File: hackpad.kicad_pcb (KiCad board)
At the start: 2 copper layers, 79 x 101 mm, 50 parts, among them J1 Conn_01x04, SW1 SW_Push, SW10 SW_Push, SW11 SW_Push, SW12 SW_Push, SW13 SW_Push, SW14 SW_Push, SW15 SW_Push, SW16 SW_Push, SW2 SW_Push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

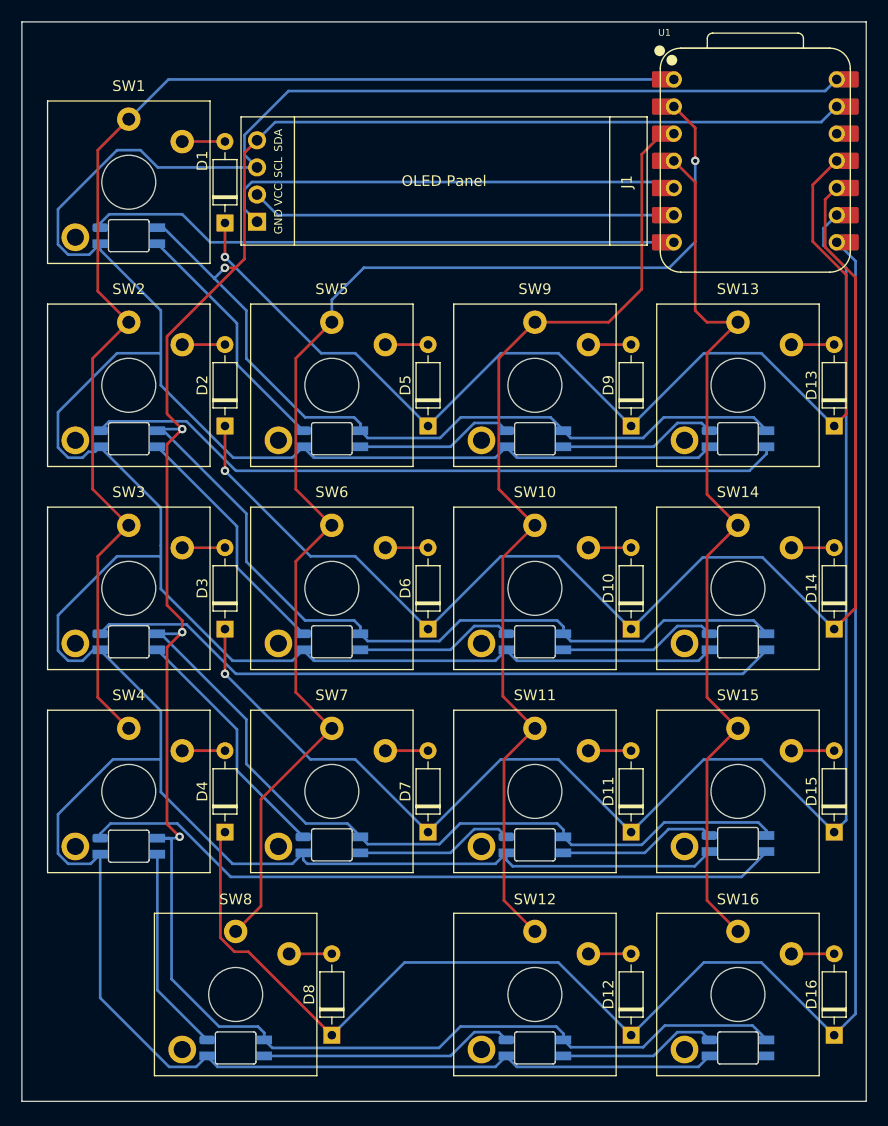
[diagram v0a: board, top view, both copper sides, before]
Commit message: add branding to pcb
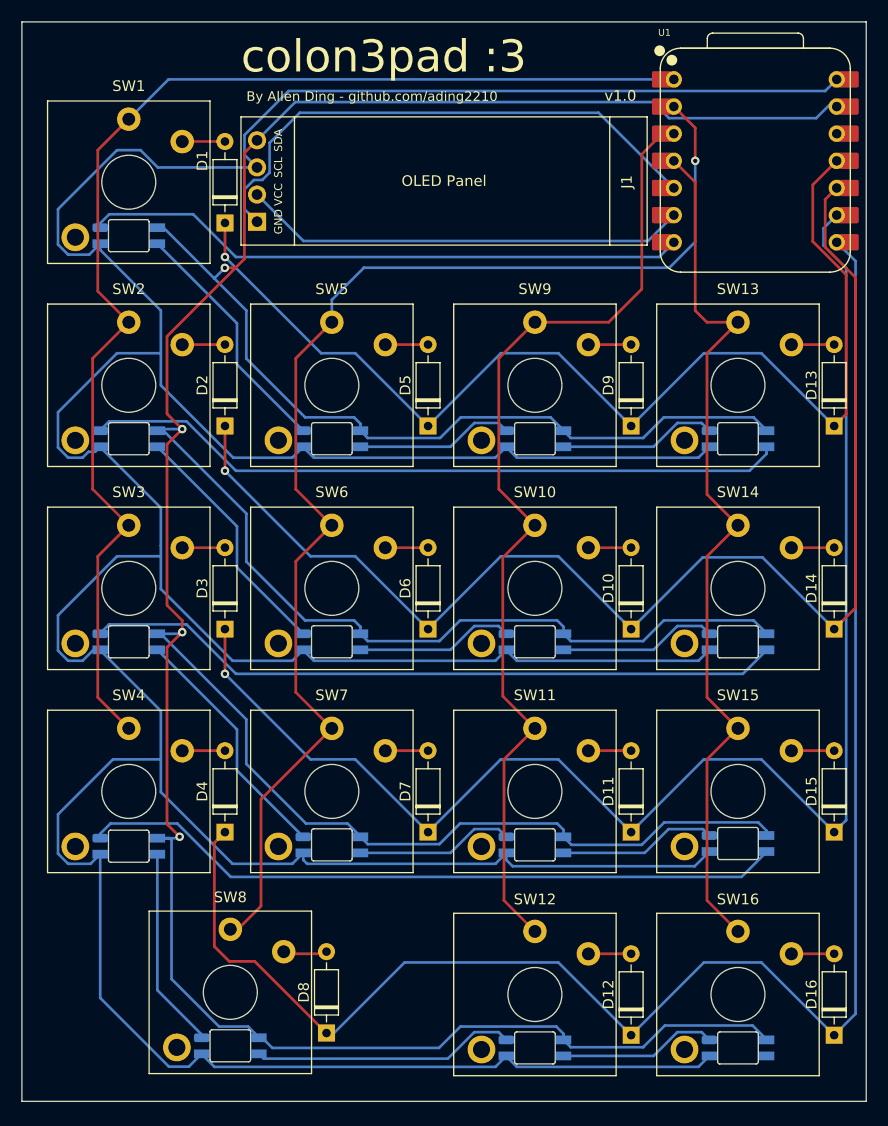
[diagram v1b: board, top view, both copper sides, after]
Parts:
- added G***: LOGO, LOGO, B.Cu at (113.5, 53.5)
- moved D24 0.54 mm to (92.5, 134.8)
- moved D8 0.54 mm to (101.5, 133.6)
- moved SW8 0.54 mm to (92.5, 129.8)
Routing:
- net /SDA: track 44.6 -> 51.6 mm
- net /SCL: track 39.8 -> 41.8 mm
- net GND: track 426.5 -> 427.7 mm
- net /DATA: track 55.5 -> 56.7 mm
- net Net-(D24-DOUT): track 23.9 -> 24.7 mm
- net /ROW4: track 158.3 -> 159.0 mm
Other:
- board text added: "By Allen Ding - github.com/ading2210"
- board text added: "blahaj :3"
- board text added: "colon3pad :3"
- board text added: "v1.0"

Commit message: add 3d models to pcb
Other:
- board size 79 x 101 mm -> 79 x 99 mm

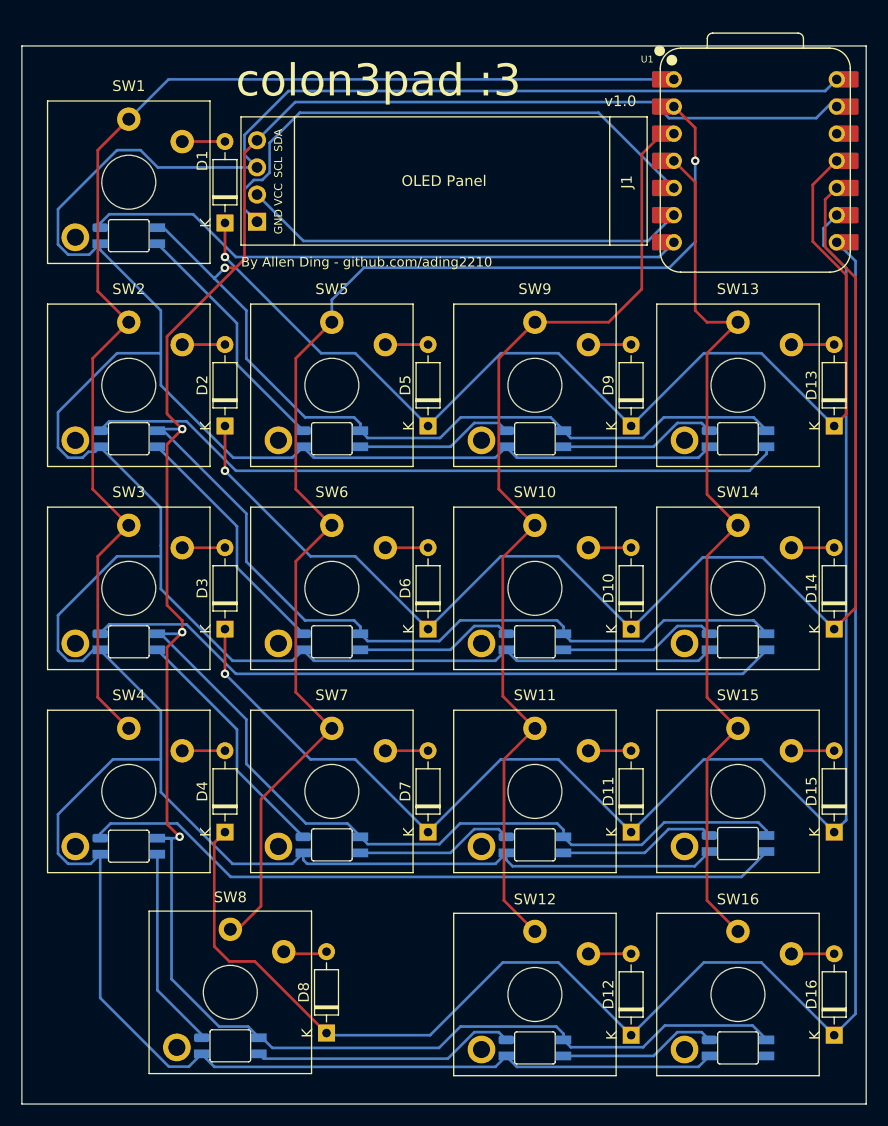
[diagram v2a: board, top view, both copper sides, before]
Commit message: rotate all key switches and redo routing
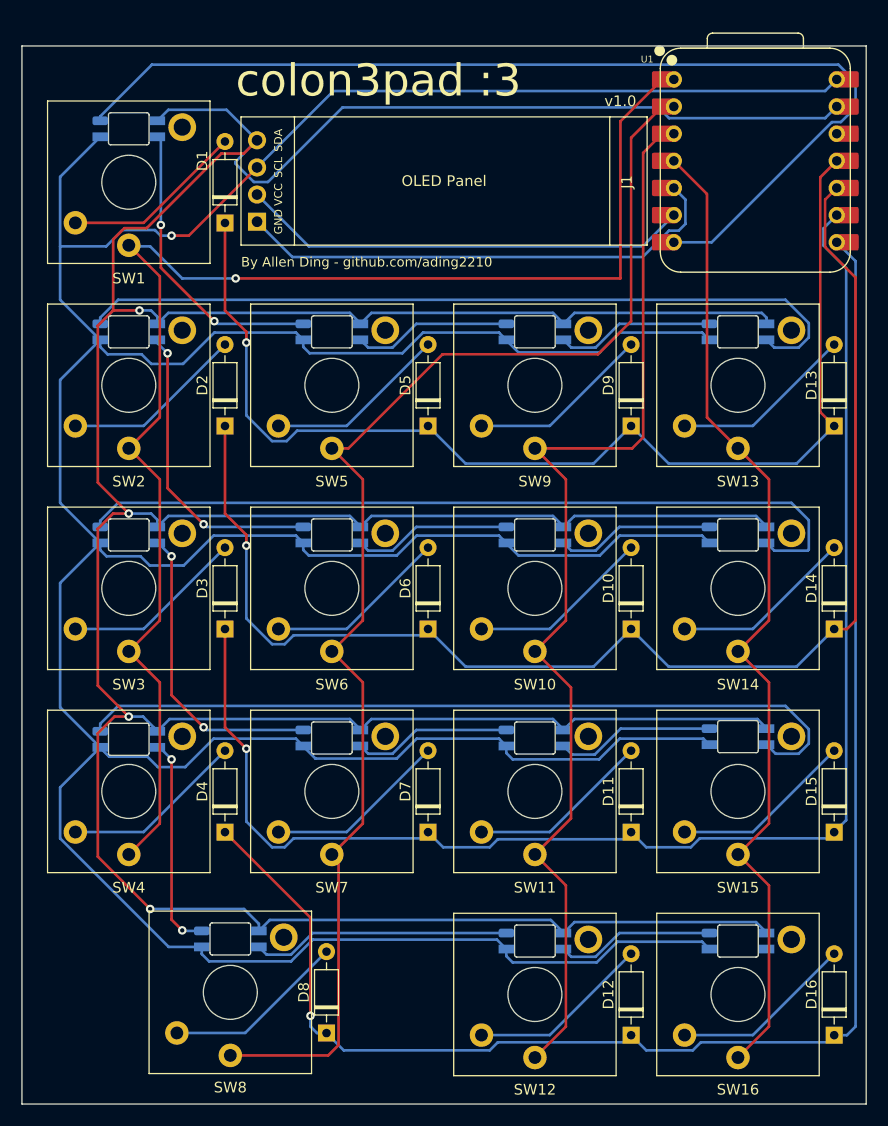
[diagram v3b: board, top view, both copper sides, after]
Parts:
- moved D24 10.0 mm to (92.5, 124.8)
- moved D17 10.0 mm to (83.0, 49.0)
- moved D18 10.0 mm to (83.0, 68.0)
- moved D19 10.0 mm to (83.0, 87.0)
- moved D20 10.0 mm to (83.0, 106.1)
- moved D21 10.0 mm to (102.0, 68.0)
- moved D22 10.0 mm to (102.0, 87.0)
- moved D23 10.0 mm to (102.0, 106.0)
- moved D25 10.0 mm to (121.0, 68.0)
- moved D26 10.0 mm to (121.0, 87.0)
- moved D27 10.0 mm to (121.0, 106.0)
- moved D28 10.0 mm to (121.0, 125.0)
- moved D29 10.0 mm to (140.0, 68.0)
- moved D30 10.0 mm to (140.0, 87.0)
- moved D31 10.0 mm to (140.0, 105.9)
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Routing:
- net /DATA: track 56.7 -> 98.4 mm
- net +5V: track 443.1 -> 414.4 mm, vias 0 -> 1
- net /COL1: track 117.1 -> 132.8 mm, vias 0 -> 1
- net Net-(D12-A): track 4.00 -> 17.2 mm
- net Net-(D16-A): track 4.00 -> 17.2 mm
- net Net-(D8-A): track 4.00 -> 17.2 mm
- net Net-(D7-A): track 4.00 -> 17.2 mm
- net Net-(D6-A): track 4.00 -> 17.2 mm
- net Net-(D5-A): track 4.00 -> 17.2 mm
- net Net-(D4-A): track 4.00 -> 17.2 mm
- net Net-(D3-A): track 4.00 -> 17.2 mm
- net Net-(D2-A): track 4.00 -> 17.2 mm
- net Net-(D11-A): track 4.00 -> 17.2 mm
- net Net-(D1-A): track 4.00 -> 17.2 mm
- net Net-(D9-A): track 4.00 -> 17.2 mm
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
